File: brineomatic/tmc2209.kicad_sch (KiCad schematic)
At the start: 17 parts, among them J20 Conn_01x04, U9 TMC2209-LA

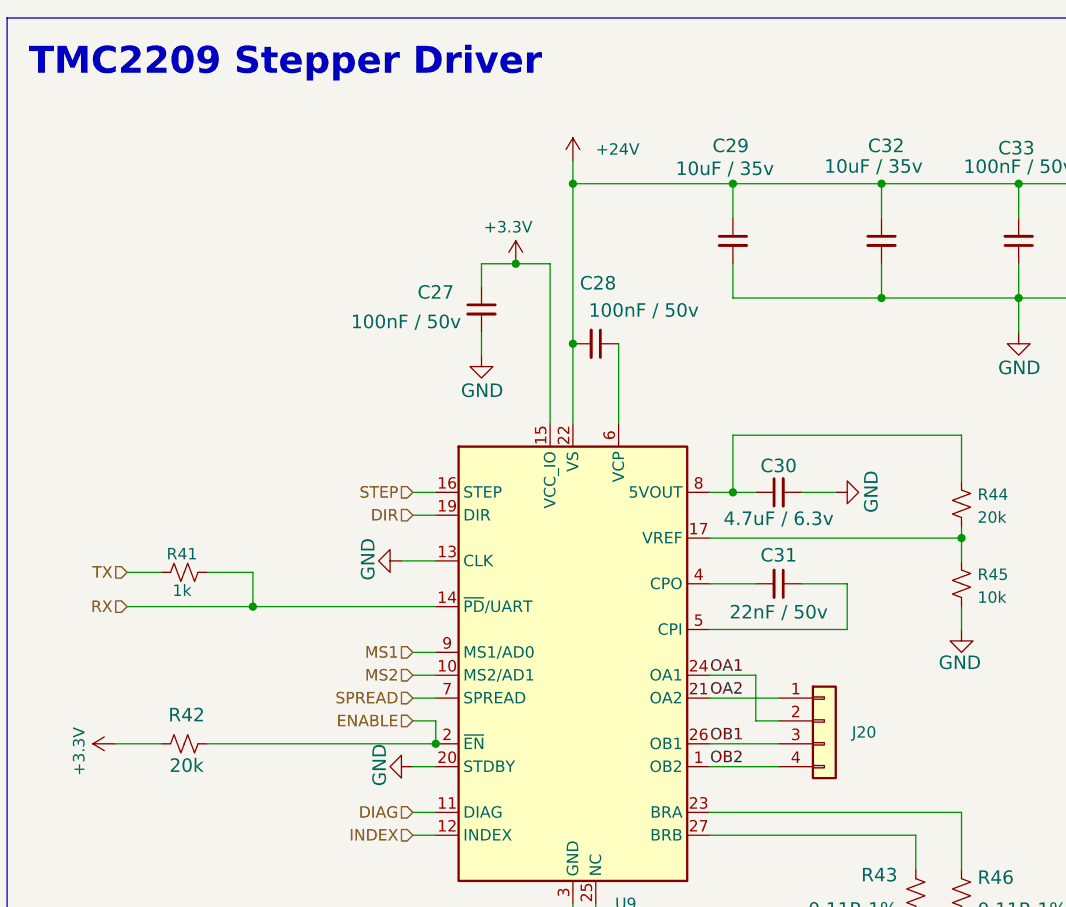
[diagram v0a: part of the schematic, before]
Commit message: added back up usb serial converter headers
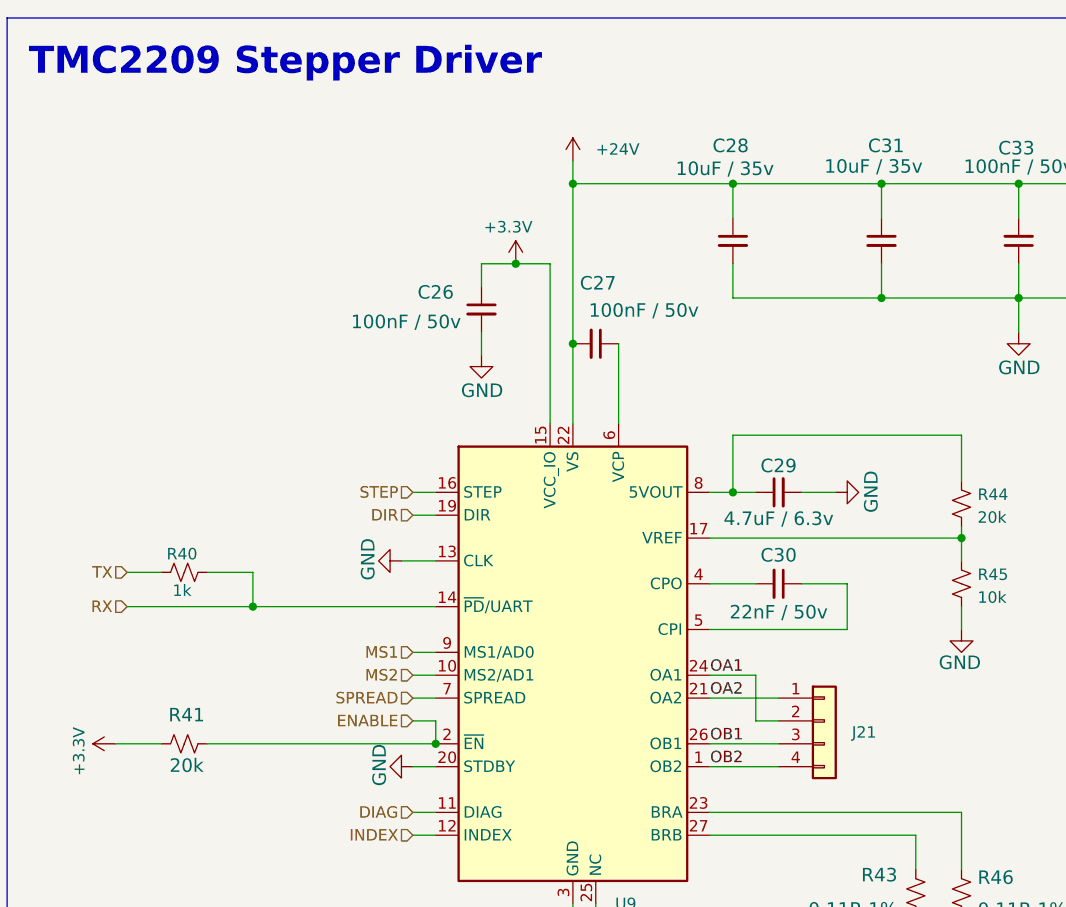
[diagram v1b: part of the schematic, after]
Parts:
- renumbered C27 to C26, C28 to C27, C29 to C28, C30 to C29, C31 to C30, C32 to C31, J20 to J21, R41 to R40, R42 to R41
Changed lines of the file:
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@@
 		(on_board yes)
 		(dnp no)
-		(property "Reference" "C32"
+		(property "Reference" "C31"
 			(at 118.11 45.72 0)
 			(effects
@@
 			(project "brineomatic"
 				(path "/96477ae2-ef08-48f3-8dd4-fe4478541f68/0f01c39f-0c25-414e-9ed3-1ba09e2af0c5"
-					(reference "C32")
+					(reference "C31")
 					(unit 1)
 				)
@@
 		(on_board yes)
 		(dnp no)
-		(property "Reference" "R42"
+		(property "Reference" "R41"
 			(at 38.354 108.966 90)
 			(effects
@@
 			(project "brineomatic"
 				(path "/96477ae2-ef08-48f3-8dd4-fe4478541f68/0f01c39f-0c25-414e-9ed3-1ba09e2af0c5"
-					(reference "R42")
+					(reference "R41")
 					(unit 1)
 				)
@@
 		(on_board yes)
 		(dnp no)
-		(property "Reference" "C28"
+		(property "Reference" "C27"
 			(at 84.074 62.738 90)
 			(effects
@@
 			(project "brineomatic"
 				(path "/96477ae2-ef08-48f3-8dd4-fe4478541f68/0f01c39f-0c25-414e-9ed3-1ba09e2af0c5"
-					(reference "C28")
+					(reference "C27")
 					(unit 1)
 				)
@@
 		(on_board yes)
 		(dnp no)
-		(property "Reference" "R41"
+		(property "Reference" "R40"
 			(at 37.846 91.948 90)
 			(effects
@@
 			(project "brineomatic"
 				(path "/96477ae2-ef08-48f3-8dd4-fe4478541f68/0f01c39f-0c25-414e-9ed3-1ba09e2af0c5"
-					(reference "R41")
+					(reference "R40")
 					(unit 1)
 				)
@@
 		(on_board yes)
 		(dnp no)
-		(property "Reference" "C29"
+		(property "Reference" "C28"
 			(at 100.838 45.72 0)
 			(effects
@@
 			(project "brineomatic"
 				(path "/96477ae2-ef08-48f3-8dd4-fe4478541f68/0f01c39f-0c25-414e-9ed3-1ba09e2af0c5"
-					(reference "C29")
+					(reference "C28")
 					(unit 1)
 				)
@@
 		(on_board yes)
 		(dnp no)
-		(property "Reference" "J20"
+		(property "Reference" "J21"
 			(at 112.268 111.76 0)
 			(effects
@@
 			(project ""
 				(path "/96477ae2-ef08-48f3-8dd4-fe4478541f68/0f01c39f-0c25-414e-9ed3-1ba09e2af0c5"
-					(reference "J20")
+					(reference "J21")
 					(unit 1)
 				)
@@
 		(on_board yes)
 		(dnp no)
-		(property "Reference" "C27"
+		(property "Reference" "C26"
 			(at 66.04 63.754 0)
 			(effects
@@
 			(project "brineomatic"
 				(path "/96477ae2-ef08-48f3-8dd4-fe4478541f68/0f01c39f-0c25-414e-9ed3-1ba09e2af0c5"
-					(reference "C27")
+					(reference "C26")
 					(unit 1)
 				)
@@
 		(on_board yes)
 		(dnp no)
-		(property "Reference" "C31"
+		(property "Reference" "C30"
 			(at 104.14 92.964 90)
 			(effects
@@
 			(project "brineomatic"
 				(path "/96477ae2-ef08-48f3-8dd4-fe4478541f68/0f01c39f-0c25-414e-9ed3-1ba09e2af0c5"
-					(reference "C31")
+					(reference "C30")
 					(unit 1)
 				)
@@
 		(on_board yes)
 		(dnp no)
-		(property "Reference" "C30"
+		(property "Reference" "C29"
 			(at 104.14 81.28 90)
 			(effects
@@
 			(project "brineomatic"
 				(path "/96477ae2-ef08-48f3-8dd4-fe4478541f68/0f01c39f-0c25-414e-9ed3-1ba09e2af0c5"
-					(reference "C30")
-					(unit 1)
-				)
+					(reference "C29")
+					(unit 1)
+				)

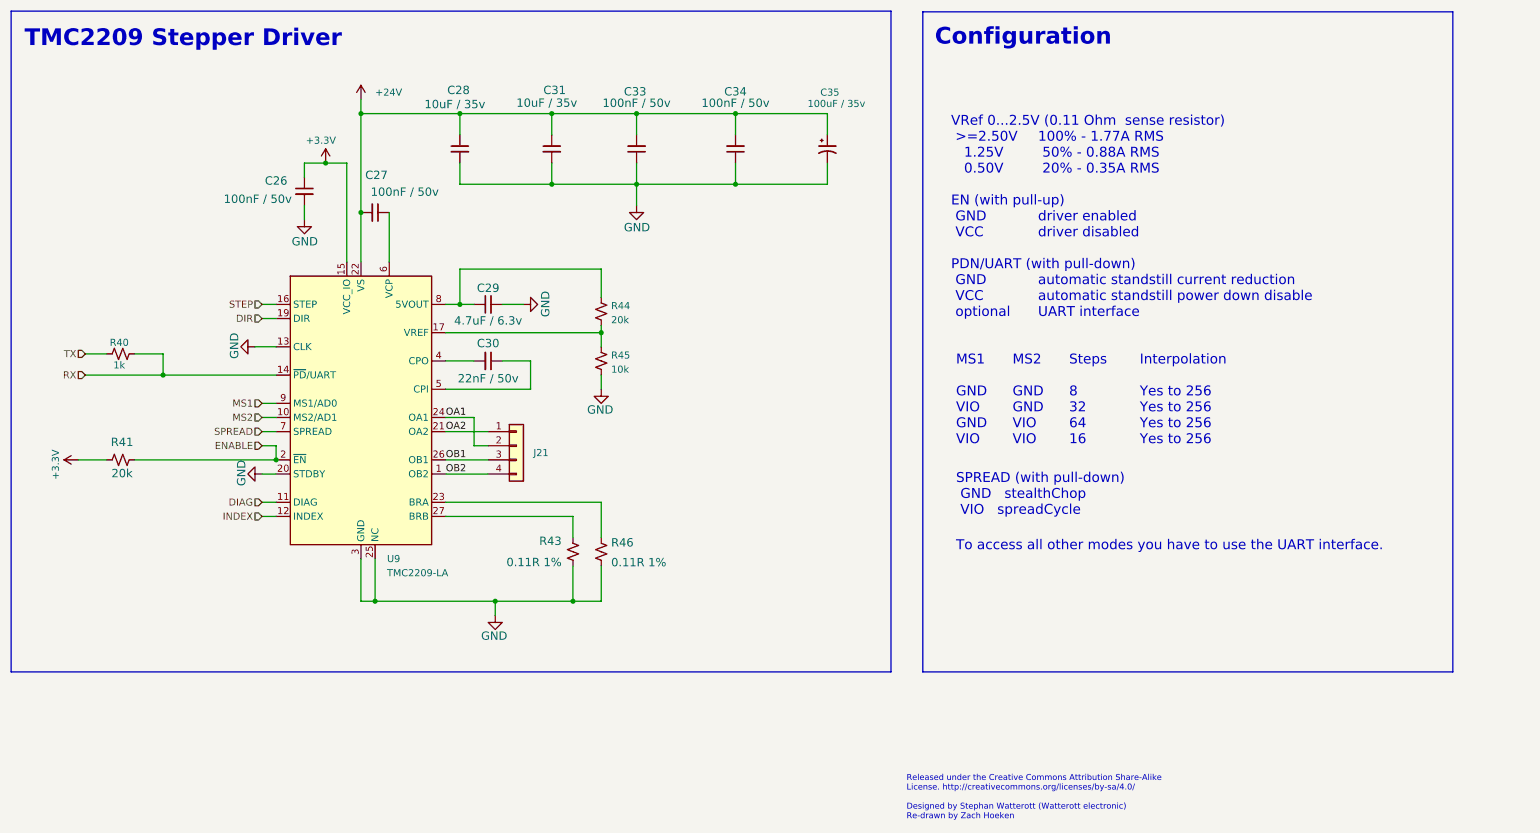
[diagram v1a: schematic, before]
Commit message: switched to the LDL1117 ldo
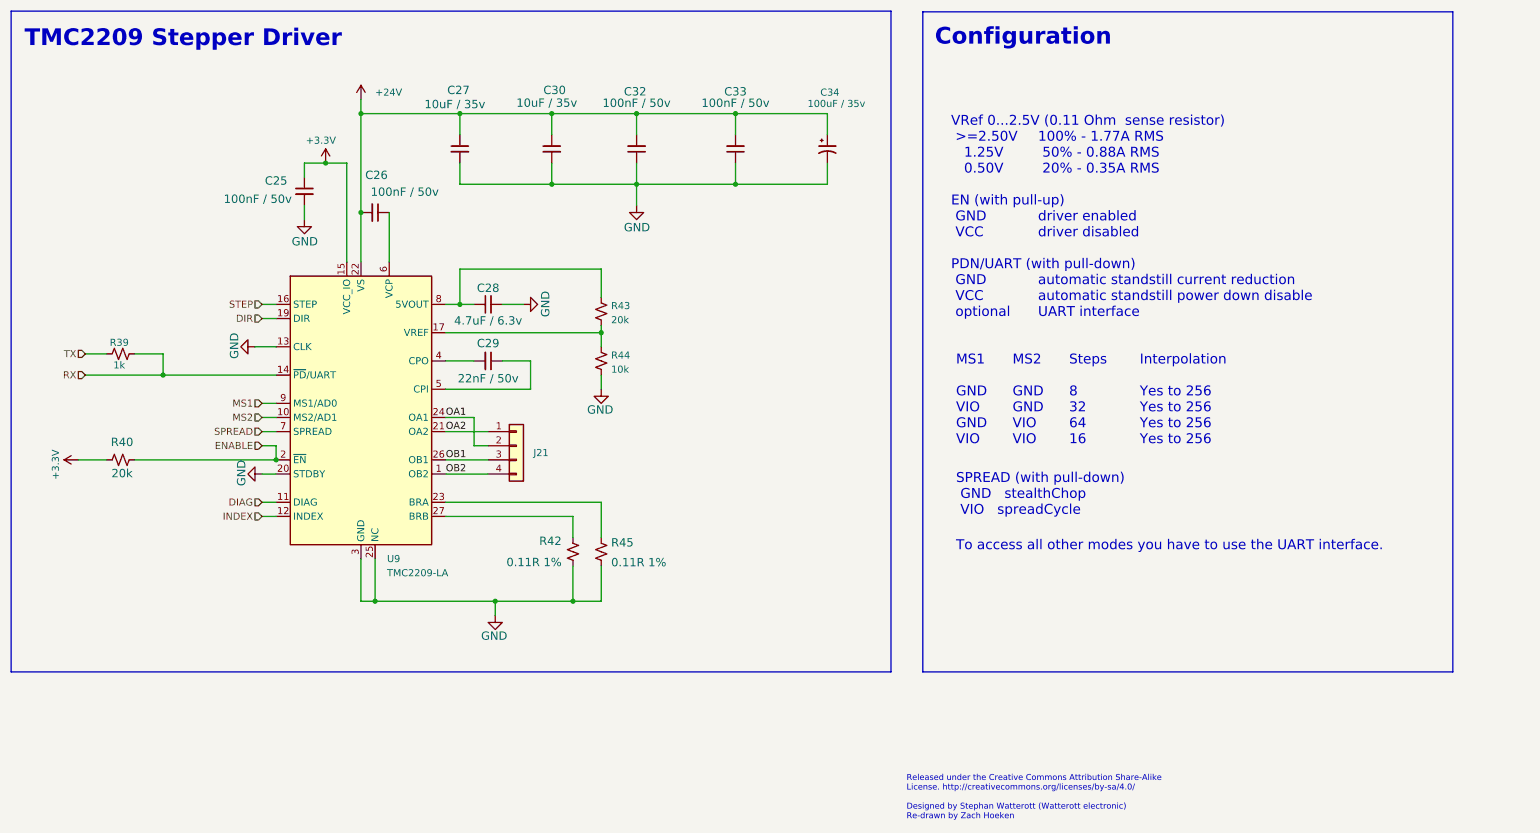
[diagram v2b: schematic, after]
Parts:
- renumbered C26 to C25, C27 to C26, C28 to C27, C29 to C28, C30 to C29, C31 to C30, C33 to C32, C34 to C33, C35 to C34, R40 to R39, R41 to R40, R43 to R42, R44 to R43, R45 to R44, R46 to R45
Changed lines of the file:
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@@
 		(on_board yes)
 		(dnp no)
-		(property "Reference" "C31"
+		(property "Reference" "C30"
 			(at 118.11 45.72 0)
 			(effects
@@
 			(project "brineomatic"
 				(path "/96477ae2-ef08-48f3-8dd4-fe4478541f68/0f01c39f-0c25-414e-9ed3-1ba09e2af0c5"
-					(reference "C31")
+					(reference "C30")
 					(unit 1)
 				)
@@
 		(on_board yes)
 		(dnp no)
-		(property "Reference" "R41"
+		(property "Reference" "R40"
 			(at 38.354 108.966 90)
 			(effects
@@
 			(project "brineomatic"
 				(path "/96477ae2-ef08-48f3-8dd4-fe4478541f68/0f01c39f-0c25-414e-9ed3-1ba09e2af0c5"
-					(reference "R41")
+					(reference "R40")
 					(unit 1)
 				)
@@
 		(on_board yes)
 		(dnp no)
-		(property "Reference" "C34"
+		(property "Reference" "C33"
 			(at 148.59 45.974 0)
 			(effects
@@
 			(project "brineomatic"
 				(path "/96477ae2-ef08-48f3-8dd4-fe4478541f68/0f01c39f-0c25-414e-9ed3-1ba09e2af0c5"
-					(reference "C34")
+					(reference "C33")
 					(unit 1)
 				)
@@
 		(on_board yes)
 		(dnp no)
-		(property "Reference" "R46"
+		(property "Reference" "R45"
 			(at 126.238 128.778 0)
 			(effects
@@
 			(project "brineomatic"
 				(path "/96477ae2-ef08-48f3-8dd4-fe4478541f68/0f01c39f-0c25-414e-9ed3-1ba09e2af0c5"
-					(reference "R46")
+					(reference "R45")
 					(unit 1)
 				)
@@
 		(on_board yes)
 		(dnp no)
-		(property "Reference" "C27"
+		(property "Reference" "C26"
 			(at 84.074 62.738 90)
 			(effects
@@
 			(project "brineomatic"
 				(path "/96477ae2-ef08-48f3-8dd4-fe4478541f68/0f01c39f-0c25-414e-9ed3-1ba09e2af0c5"
-					(reference "C27")
+					(reference "C26")
 					(unit 1)
 				)
@@
 		(on_board yes)
 		(dnp no)
-		(property "Reference" "R40"
+		(property "Reference" "R39"
 			(at 37.846 91.948 90)
 			(effects
@@
 			(project "brineomatic"
 				(path "/96477ae2-ef08-48f3-8dd4-fe4478541f68/0f01c39f-0c25-414e-9ed3-1ba09e2af0c5"
-					(reference "R40")
+					(reference "R39")
 					(unit 1)
 				)
@@
 		(on_board yes)
 		(dnp no)
-		(property "Reference" "C35"
+		(property "Reference" "C34"
 			(at 163.83 46.99 0)
 			(effects
@@
 			(project ""
 				(path "/96477ae2-ef08-48f3-8dd4-fe4478541f68/0f01c39f-0c25-414e-9ed3-1ba09e2af0c5"
-					(reference "C35")
+					(reference "C34")
 					(unit 1)
 				)
@@
 		(on_board yes)
 		(dnp no)
-		(property "Reference" "C28"
+		(property "Reference" "C27"
 			(at 100.838 45.72 0)
 			(effects
@@
 			(project "brineomatic"
 				(path "/96477ae2-ef08-48f3-8dd4-fe4478541f68/0f01c39f-0c25-414e-9ed3-1ba09e2af0c5"
-					(reference "C28")
+					(reference "C27")
 					(unit 1)
 				)
@@
 		(on_board yes)
 		(dnp no)
-		(property "Reference" "R43"
+		(property "Reference" "R42"
 			(at 117.348 126.746 0)
 			(effects
@@
 			(project "brineomatic"
 				(path "/96477ae2-ef08-48f3-8dd4-fe4478541f68/0f01c39f-0c25-414e-9ed3-1ba09e2af0c5"
-					(reference "R43")
+					(reference "R42")
 					(unit 1)
 				)
@@
 		(on_board yes)
 		(dnp no)
-		(property "Reference" "C26"
+		(property "Reference" "C25"
 			(at 66.04 63.754 0)
 			(effects
@@
 			(project "brineomatic"
 				(path "/96477ae2-ef08-48f3-8dd4-fe4478541f68/0f01c39f-0c25-414e-9ed3-1ba09e2af0c5"
-					(reference "C26")
+					(reference "C25")
 					(unit 1)
 				)
@@
 		(on_board yes)
 		(dnp no)
-		(property "Reference" "R44"
+		(property "Reference" "R43"
 			(at 126.238 85.344 0)
 			(effects
@@
 			(project "brineomatic"
 				(path "/96477ae2-ef08-48f3-8dd4-fe4478541f68/0f01c39f-0c25-414e-9ed3-1ba09e2af0c5"
-					(reference "R44")
+					(reference "R43")
 					(unit 1)
 				)
@@
 		(on_board yes)
 		(dnp no)
-		(property "Reference" "C30"
+		(property "Reference" "C29"
 			(at 104.14 92.964 90)
 			(effects
@@
 			(project "brineomatic"
 				(path "/96477ae2-ef08-48f3-8dd4-fe4478541f68/0f01c39f-0c25-414e-9ed3-1ba09e2af0c5"
-					(reference "C30")
+					(reference "C29")
 					(unit 1)
 				)
@@
 		(on_board yes)
 		(dnp no)
-		(property "Reference" "C29"
+		(property "Reference" "C28"
 			(at 104.14 81.28 90)
 			(effects
@@
 			(project "brineomatic"
 				(path "/96477ae2-ef08-48f3-8dd4-fe4478541f68/0f01c39f-0c25-414e-9ed3-1ba09e2af0c5"
-					(reference "C29")
+					(reference "C28")
 					(unit 1)
 				)
@@
 		(on_board yes)
 		(dnp no)
-		(property "Reference" "R45"
+		(property "Reference" "R44"
 			(at 126.238 94.234 0)
 			(effects
@@
 			(project "brineomatic"
 				(path "/96477ae2-ef08-48f3-8dd4-fe4478541f68/0f01c39f-0c25-414e-9ed3-1ba09e2af0c5"
-					(reference "R45")
+					(reference "R44")
 					(unit 1)
 				)
@@
 		(on_board yes)
 		(dnp no)
-		(property "Reference" "C33"
+		(property "Reference" "C32"
 			(at 130.556 45.974 0)
 			(effects
@@
 			(project "brineomatic"
 				(path "/96477ae2-ef08-48f3-8dd4-fe4478541f68/0f01c39f-0c25-414e-9ed3-1ba09e2af0c5"
-					(reference "C33")
-					(unit 1)
-				)
+					(reference "C32")
+					(unit 1)
+				)
